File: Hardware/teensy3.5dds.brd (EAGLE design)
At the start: 110 x 85 mm, 102 parts, among them IC1 AD8034, IC10 AD8034, IC11 AD8034, IC12 AD8034, IC2 AD8034, IC4 AD737KRZ-R7, IC8 AD8034, IC9 AD8034, J1 1776275-2, J2 1776275-2, Q1 CSM-7X-DU, X1 1-227161-0

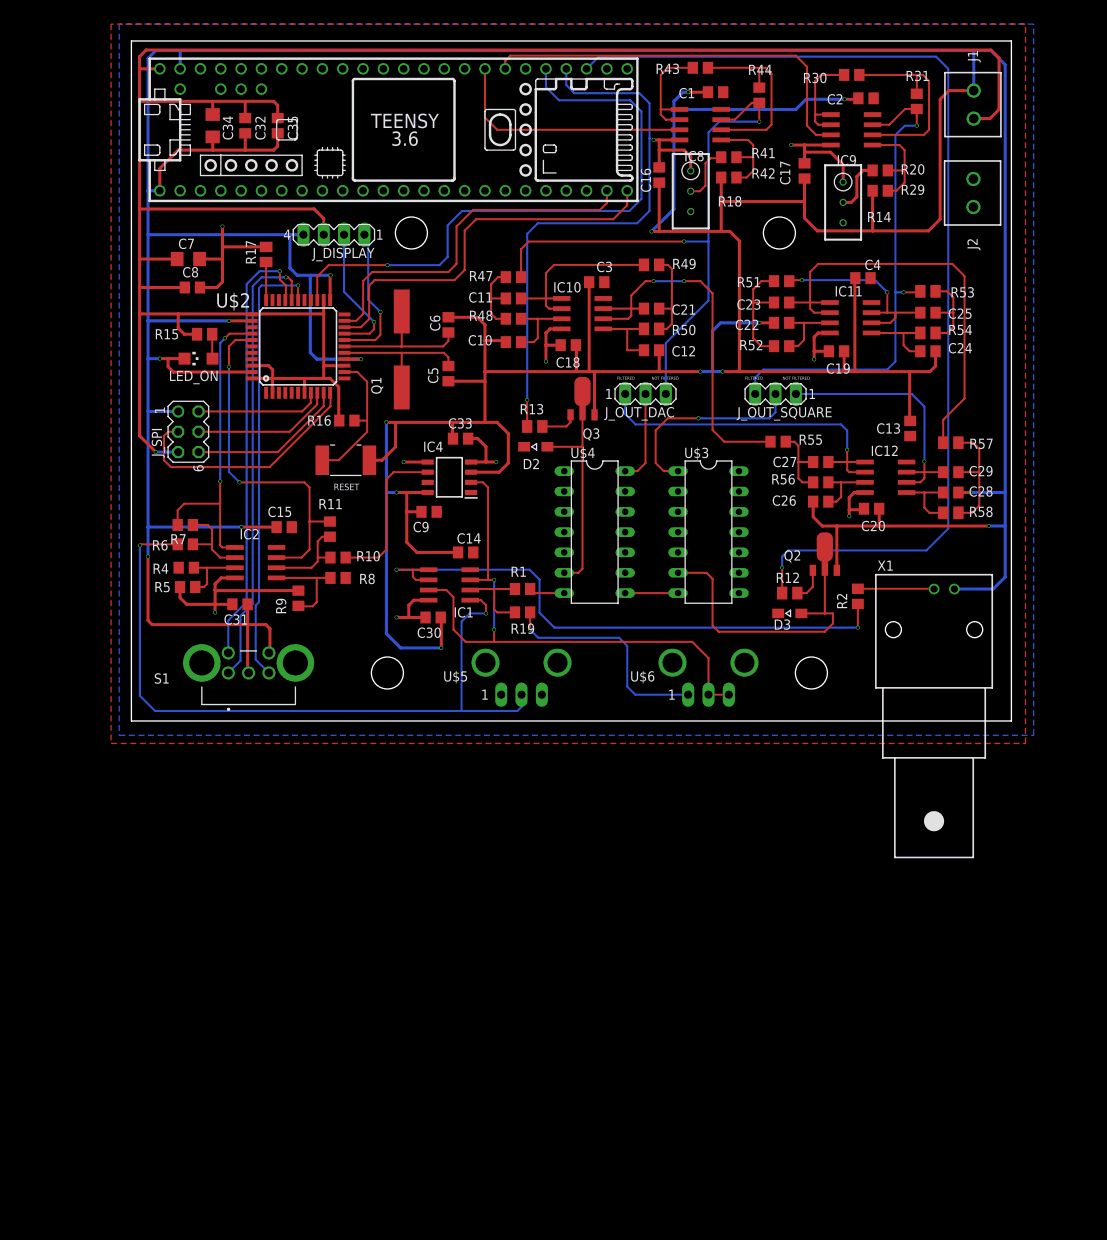
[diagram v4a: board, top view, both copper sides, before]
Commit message: hardware: renumber parts * Label power connector on board
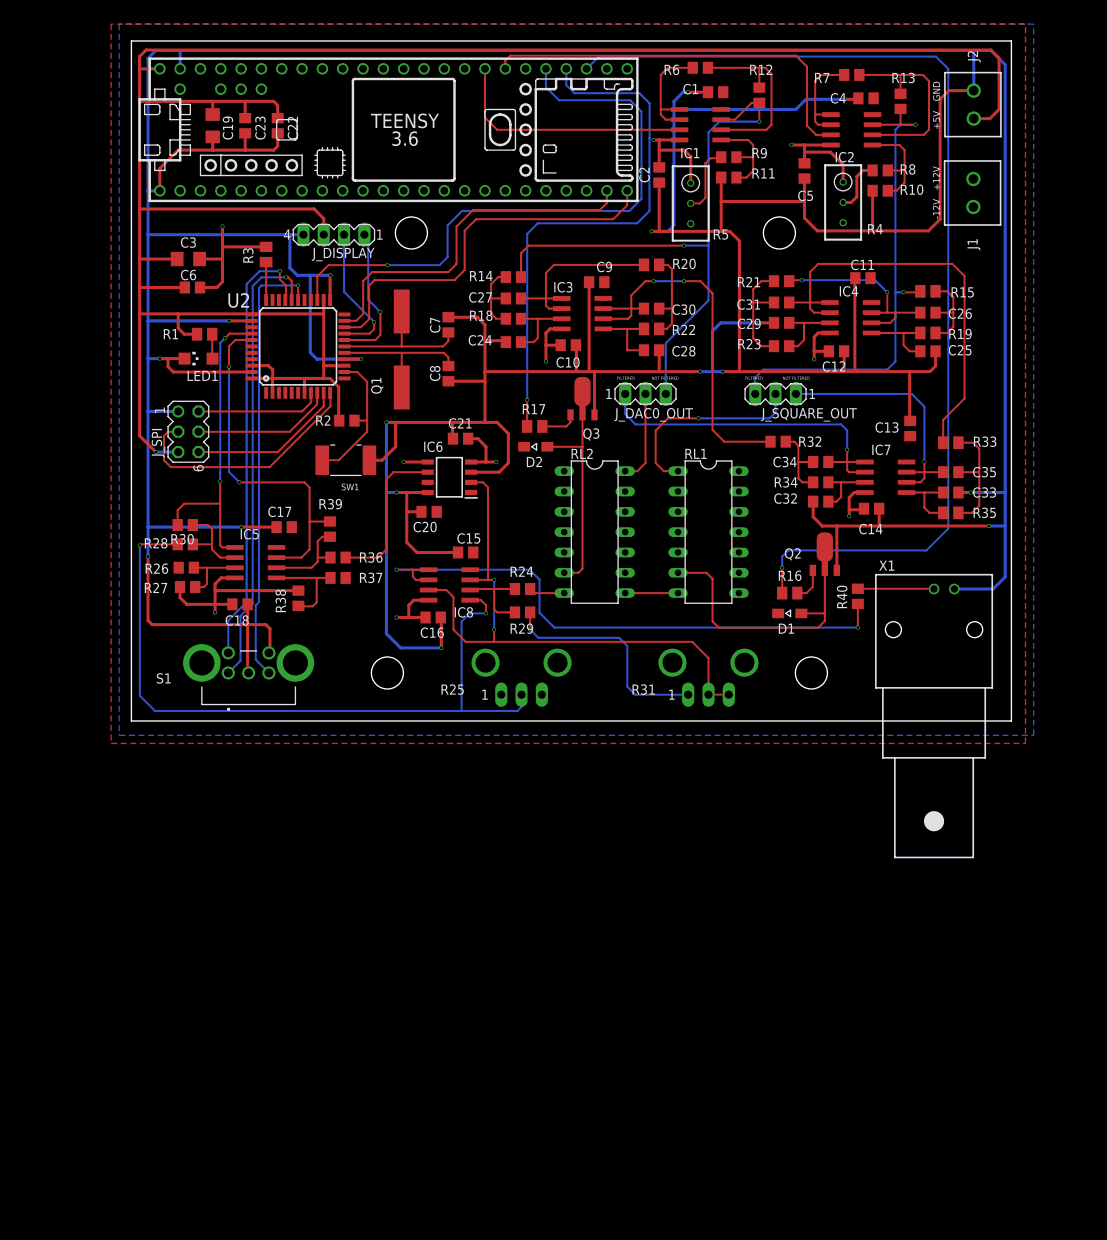
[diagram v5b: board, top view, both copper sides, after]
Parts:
- removed IC11, IC9: AD8034, linear:SO08
- removed R41, R42, R43, R44, R47, R48: (no value), rcl:R0805
- removed R49, R53, R54: (no value), rcl:M0805
- removed U$6: POTENTIOMETER_VERTICAL, Potentiometer_vertical:MA03-1
- added IC5: AD8034, linear:SO08
- added IC6: AD737KRZ-R7, AD737KRZ-R7:SOIC127P600X175-8N
- added R24, R26, R27, R28, R36, R37, R38, R39, R40: (no value), rcl:R0805
- added R3: 10kOhm, rcl:M0805
- C19: value (none) -> 100n; device rcl:C0805 -> rcl:C1206
- C22, C23: value (none) -> 100n
- C3: value (none) -> 1u; device rcl:C0805 -> rcl:C1206
- C32, C35: value 100n -> (none)
- C34: value 100n -> (none); device rcl:C1206 -> rcl:C0805
- C5: value 22pF -> (none)
- C6: value 22pF -> 1u
- C7: value 1u -> 22pF; device rcl:C1206 -> rcl:C0805
- C8: value 1u -> 22pF
- IC4: value AD737KRZ-R7 -> AD8034; device AD737KRZ-R7:SOIC127P600X175-8N -> linear:SO08
- R1: value (none) -> 220Ohm; device rcl:R0805 -> rcl:M0805
- R12, R13: device rcl:M0805 -> rcl:R0805
- R14, R18: device rcl:RTRIM3296W -> rcl:R0805
- R15: value 220Ohm -> (none)
- R16: value 10kOhm -> (none); device rcl:R0805 -> rcl:M0805
- R17: value 10kOhm -> (none)
- R19, R20: device rcl:R0805 -> rcl:M0805
- R2: value (none) -> 10kOhm
- R31: value (none) -> POTENTIOMETER_VERTICAL; device rcl:R0805 -> Potentiometer_vertical:MA03-1
- R4, R5: device rcl:R0805 -> rcl:RTRIM3296W
- moved R30 100.5 mm to (6.73, 39.5), turned to 0 degrees
- moved R7 100.5 mm to (90.0, 95.8), turned to 180 degrees
- moved C35 94.6 mm to (102.4, 46.1), turned to 180 degrees
- moved R4 93.9 mm to (89.0, 79.8)
- moved IC2 92.1 mm to (90.0, 88.9)
- moved R15 90.6 mm to (99.6, 68.7), turned to 0 degrees
- moved R6 87.7 mm to (71.1, 96.6), turned to 180 degrees
- moved C34 86.9 mm to (86.2, 47.4), turned to 180 degrees
- moved C32 85.9 mm to (86.2, 42.4), turned to 0 degrees
- moved R8 84.8 mm to (93.6, 83.8), turned to 0 degrees
- moved C19 82.9 mm to (10.2, 89.4), turned to 270 degrees
- moved R10 81.8 mm to (93.6, 81.3), turned to 0 degrees
- moved R5 79.1 mm to (69.9, 79.7), turned to 180 degrees
- moved C17 78.8 mm to (19.1, 39.2), turned to 180 degrees
- moved R31 78.6 mm to (72.1, 18.3), turned to 0 degrees
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- renumbered D3 to D1, IC10 to IC3, IC12 to IC7, J_OUT_DAC to J_DAC0_OUT, J_OUT_SQUARE to J_SQUARE_OUT, LED_ON to LED1, R50 to R22, R51 to R21, R52 to R23, R55 to R32, R56 to R34, R57 to R33, R58 to R35, RESET to SW1, U$1 to U1, U$2 to U2, U$3 to RL1, U$4 to RL2, U$5 to R25
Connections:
- net +5V: now also C19.1, C22.1, C23.1, C3.1, C6.1, J2.1, R1.2, R2.2; no longer C32.1, C34.1, C35.1, C7.1, C8.1, J1.1, R15.2, R16.2
- net AMPL_MEASURE: now also IC5.7, R39.2; no longer IC2.7, R11.2
- net DAC0: now also IC1.3; no longer IC8.3
- net DAC0_FILTERED: now also C34.1; no longer C27.1
- net DAC0_OFFSET: now also IC1.7, R12.1, R14.1; no longer IC8.7, R44.1, R47.1
- net DAC0_SEL: now also R17.1; no longer R13.1
- net GND: now also C11.2, C14.1, C17.2, C19.2, C2.1, C20.2, C21.1, C22.2, C23.2, C25.1, C29.1, C32.1, C6.2, C7.1, C8.1, IC6.3, IC6.8, J2.2, R10.1, R11.1, R3.2; no longer C14.2, C17.1, C19.1, C2.2, C20.1, C22.1, C26.1, C30.1, C31.1, C32.2, C34.2, C35.2, C6.1, C7.2, C8.2, IC4.3, IC4.8, J1.2, R17.2, R29.1, R42.1
- net N$10: now also R24.1; no longer R1.1
- net N$11: now also IC5.2, R28.2, R30.2; no longer IC2.2, R6.2, R7.2
- net N$13: now also IC5.3, R26.1, R27.2; no longer IC2.3, R4.1, R5.2
- net N$14: now also IC6.6, R36.1; no longer IC4.6, R10.1
- net N$15: now also R29.2, R31.1; no longer R19.2, U$6.1
- net N$16: now also IC5.6, R36.2, R39.1; no longer IC2.6, R10.2, R11.1
- net N$17: now also R16.2; no longer R12.2
- net N$18: now also R17.2; no longer R13.2
- net N$19: now also IC8.1, IC8.2, R40.1; no longer IC1.1, IC1.2, R2.1
- net N$22: now also IC5.5, R37.2, R38.1; no longer IC2.5, R8.2, R9.1
- net N$3: now also IC8.5, R28.1; no longer IC1.5, R6.1
- net N$30: now also R1.1; no longer R15.1
- net N$31: now also C7.2; no longer C6.2
- net N$32: now also R3.1; no longer R17.1
- net N$35: now also R2.1; no longer R16.1
- net N$38: now also IC2.1, IC2.2, R7.2; no longer IC9.1, IC9.2, R30.2
- net N$4: now also C8.2; no longer C5.2
- net N$41: now also IC1.1, IC1.2, R6.2; no longer IC8.1, IC8.2, R43.2
- net N$5: now also IC8.6, R24.2, R29.1; no longer IC1.6, R1.2, R19.1
- net N$50: now also C27.2, R14.2, R18.1; no longer C11.2, R47.2, R48.1
- net N$51: now also IC1.6, R12.2, R6.1; no longer IC8.6, R43.1, R44.2
- net N$53: now also C27.1, R20.1; no longer C11.1, R49.1
- net N$54: now also IC1.5, R11.2, R9.2; no longer IC8.5, R41.2, R42.2
- net N$56: now also R5.2, R9.1; no longer R18.2, R41.1
- net N$57: now also IC2.6, R13.2, R7.1; no longer IC9.6, R30.1, R31.2
- net N$58: now also C24.2, R18.2; no longer C10.2, R48.2
- net N$59: now also IC2.5, R10.2, R8.2; no longer IC9.5, R20.2, R29.2
- net N$6: now also R40.2; no longer R2.2
- net N$60: now also R4.2, R8.1; no longer R14.2, R20.1
- net N$61: now also C30.1, R20.2; no longer C21.1, R49.2
- net N$62: now also C30.2; no longer C21.2
- net N$63: now also C28.2; no longer C12.2
- net N$66: now also C31.2; no longer C23.2
- net N$67: now also C31.1, IC4.1, IC4.2; no longer C23.1, IC11.1, IC11.2
- net N$68: now also C29.2, IC4.3; no longer C22.2, IC11.3
- net N$69: now also C26.1, R15.2, R19.1; no longer C25.1, R53.2, R54.1
- net N$70: now also C26.2, IC4.6, IC4.7; no longer C25.2, IC11.6, IC11.7
- net N$71: now also C25.2, IC4.5, R19.2; no longer C24.2, IC11.5, R54.2
- net N$73: now also C34.2; no longer C27.2
- net N$75: now also C32.2; no longer C26.2
- net N$76: now also C35.1; no longer C29.1
- net N$78: now also C33.2; no longer C28.2
- net N$9: now also IC6.2, IC8.3, IC8.7, R31.2, R31.3; no longer IC1.3, IC1.7, IC4.2, U$6.2, U$6.3
- net OFF_MEASURE: now also IC5.1, R30.1; no longer IC2.1, R7.1
- net SQUARE: now also IC2.3; no longer IC9.3
- net SQUARE_FILTERED: now also C35.2; no longer C29.2
- net SQUARE_OFFSET: now also IC2.7, R13.1, R15.1; no longer IC9.7, R31.1, R53.1
- net SQUARE_SEL: now also R16.1; no longer R12.1
- net V+: now also C11.1, C17.1, C20.1, IC4.8, IC5.8, IC6.7, J1.2, R26.2, R37.1, R4.3, R5.3; no longer C14.1, C2.1, C3.1, IC11.8, IC4.7, IC9.8, J2.2, R14.3, R18.3, R4.2, R8.1
- net V-: now also C10.2, C12.2, C14.2, C2.2, C21.2, C5.2, IC5.4, IC6.4, IC6.5, J1.1, R27.1, R38.2, R4.1; no longer C17.2, C19.2, C20.2, C30.2, C31.2, C33.2, IC11.4, IC4.5, IC9.4, J2.1, R14.1, R18.1, R9.2
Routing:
- net N$2: track 37.1 -> 34.2 mm
- net V-: track 92.1 -> 93.6 mm
- net N$56: track 7.21 -> 8.74 mm
- net GND: track 844.5 -> 845.6 mm
- net SQUARE_OFFSET: track 63.5 -> 62.7 mm
- net DAC0_OFFSET: track 77.1 -> 76.6 mm
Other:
- board text added: "+12V"
- board text added: "+5V"
- board text added: "-12V"
- board text added: "GND"

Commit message: little fixes
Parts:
- added R41, R42, R43: (no value), rcl:R0805
- C1, C10, C12, C13, C14, C15, C16, C17, C18, C2, C20, C21, C4, C5, C9: value (none) -> 100n
- C23: value 100n -> 1u
- C24, C25, C28, C29, C32, C33: value (none) -> 10p
- C26, C27, C30, C31, C34, C35: value (none) -> 100p
- C6: value 1u -> 100n
- C7, C8: value 22pF -> 22p
- Q1: value CSM-7X-DU -> 10MHz
- R1: value 220Ohm -> 220
- R10, R11, R12, R24, R6, R7, R8, R9: value (none) -> 1k
- R13: value (none) -> 100k; device rcl:R0805 -> rcl:RTRIM3296W
- R14, R18: value (none) -> 2.74k
- R15: value (none) -> 130
- R19: value (none) -> 4.75k
- R2, R3: value 10kOhm -> 10k
- R20: value (none) -> 787
- R21: value (none) -> 150
- R22: value (none) -> 14.3k
- R23: value (none) -> 3.74k
- R25, R31: value POTENTIOMETER_VERTICAL -> 10k
- R29: value (none) -> 100
- R32: value (none) -> 562
- R33: value (none) -> 243
- R34: value (none) -> 20k
- R35: value (none) -> 1.78k
- R4: value (none) -> 1k; device rcl:RTRIM3296W -> rcl:R0805
- R40: value (none) -> 50
- R5: value (none) -> 100k
- moved R7 147.8 mm to (3.56, -24.1), turned to 0 degrees
- moved R8 137.9 mm to (7.75, -24.1)
- moved IC2 137.9 mm to (1.91, -17.1), turned to 0 degrees
- moved R4 137.2 mm to (-0.64, -24.1), turned to 0 degrees
- moved R13 137.0 mm to (1.91, -6.99), turned to 0 degrees
- moved R10 128.7 mm to (8.38, -15.1)
- moved S1 44.0 mm to (-7.49, -17.9), turned to 0 degrees
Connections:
- removed net N$1: S1.3, U2.28
- removed net N$38: IC2.1, IC2.2, R7.2
- removed net N$41: IC1.1, IC1.2, R6.2
- removed net N$57: IC2.6, R13.2, R7.1
- removed net N$59: IC2.5, R10.2, R8.2
- removed net N$60: R4.2, R8.1
- new net N$20: R13.2, R4.1
- new net N$23: IC1.1, IC1.2, R11.1
- new net N$24: IC2.6, R10.2, R8.1
- new net N$27: IC2.1, IC2.2, R7.1
- new net N$28: IC2.5, R4.2, R7.2
- new net N$29: R43.2, S1.5, U2.29
- new net V-1: R13.1
- net +5V: now also R41.1, R42.1
- net GND: now also R43.1, R6.2, R8.2, S1.6, S1.7; no longer R10.1, R11.1
- net N$25: now also R41.2, S1.1; no longer S1.5
- net N$8: now also R42.2, S1.3, U2.12; no longer S1.1, U2.29
- net SQUARE_OFFSET: now also R10.1; no longer R13.1
- net V+: now also R13.3; no longer R4.3
- net V-: no longer R4.1
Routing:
- net N$8: track 57.5 -> 0.00 mm, vias 1 -> 0
- net N$25: track 55.8 -> 0.00 mm, vias 1 -> 0
- net N$1: track 55.8 -> 0.00 mm, vias 1 -> 0
- net N$57: track 24.8 -> 0.00 mm
- net N$21: track 23.6 -> 0.00 mm
- net N$41: track 14.3 -> 0.00 mm
- net GND: track 845.6 -> 831.8 mm
- net N$38: track 13.1 -> 0.00 mm
- net N$59: track 12.9 -> 0.00 mm
- net N$26: track 12.0 -> 0.00 mm
- net N$23: track 0.00 -> 7.45 mm
- net N$60: track 6.83 -> 0.00 mm
- net SQUARE_OFFSET: track 62.7 -> 57.1 mm
- net DAC0_OFFSET: track 76.6 -> 73.3 mm
- net N$70: track 25.5 -> 22.9 mm
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
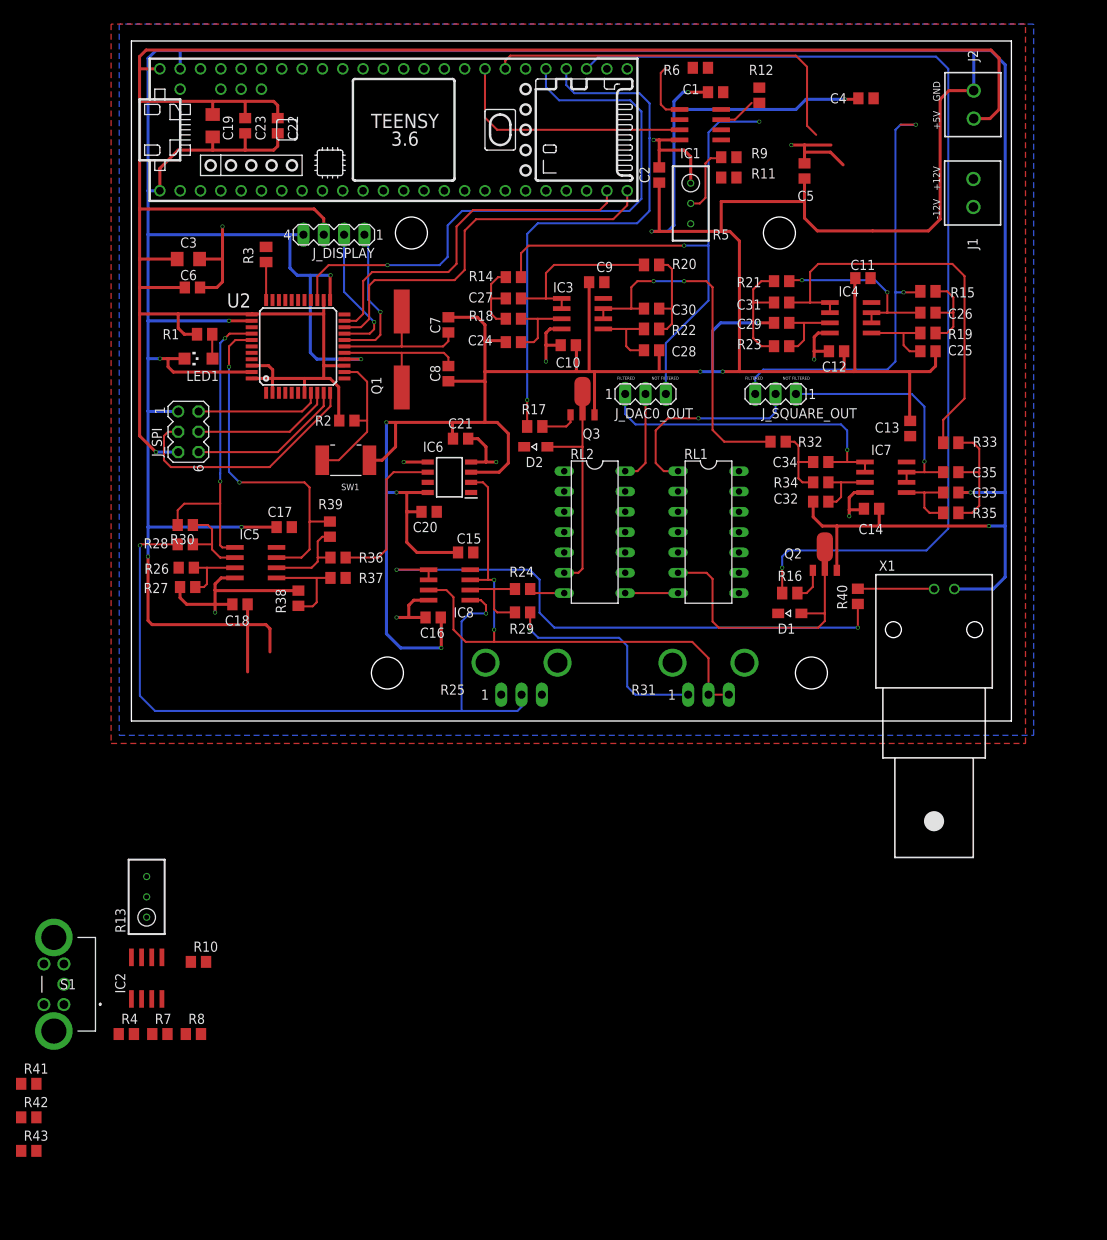
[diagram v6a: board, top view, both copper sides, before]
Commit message: an actually working filter for the square wave
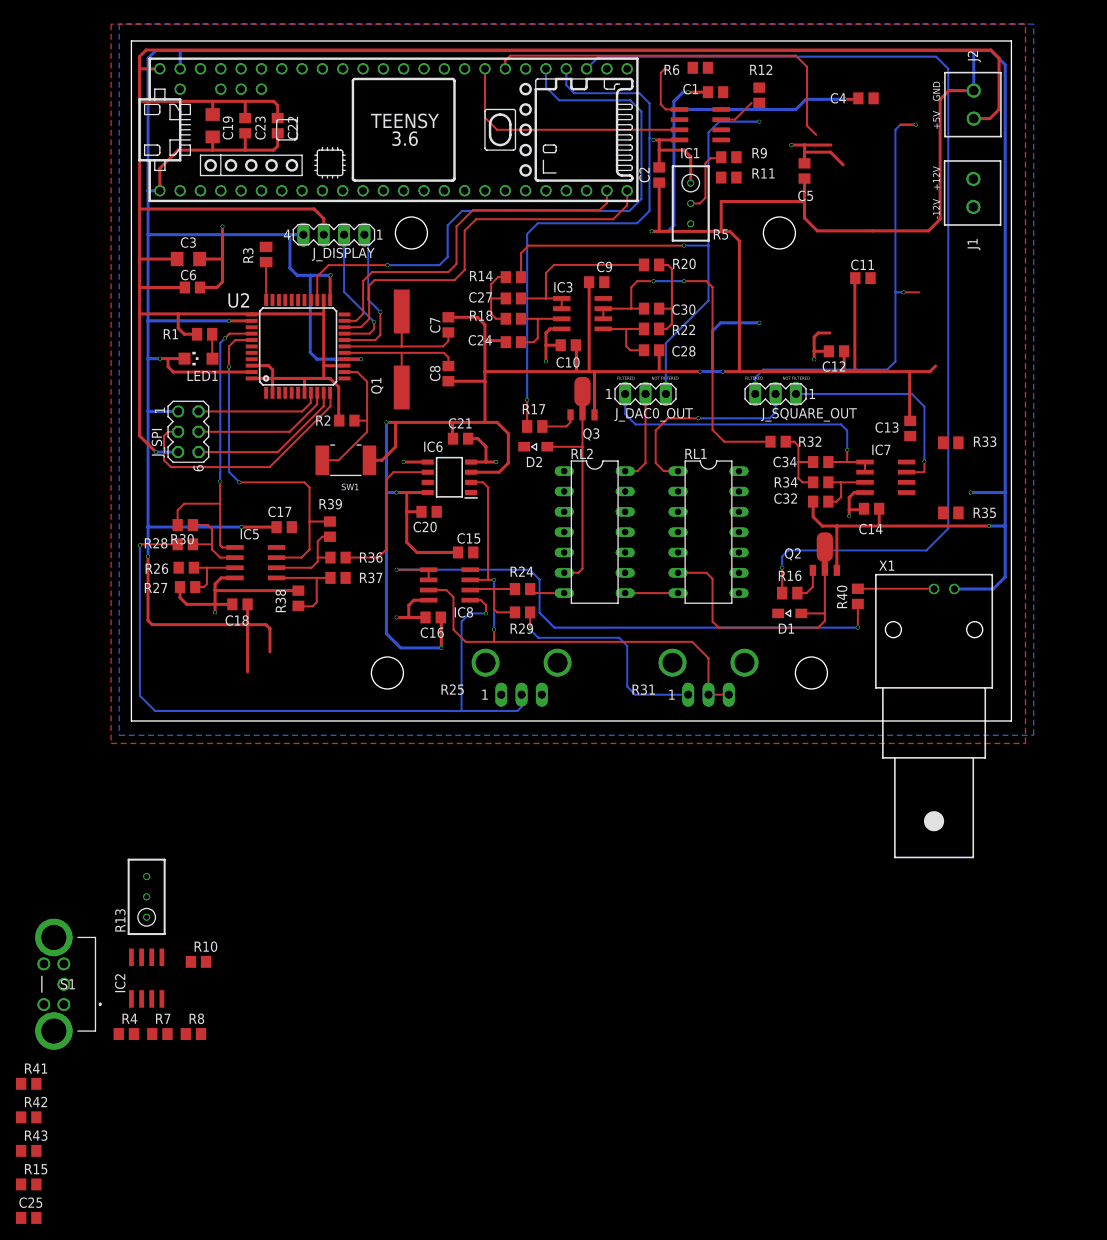
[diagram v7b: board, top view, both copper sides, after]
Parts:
- removed C26, C31, C35: 100p, rcl:C0805
- removed C29, C33: 10p, rcl:C0805
- removed IC4: AD8034, linear:SO08
- removed R19: 4.75k, rcl:M0805
- removed R21: 150, rcl:R0805
- removed R23: 3.74k, rcl:R0805
- C25: value 10p -> (none)
- R15: value 130 -> (none); device rcl:M0805 -> rcl:R0805
- moved R15 158.4 mm to (-12.8, -42.9)
- moved C25 156.1 mm to (-12.8, -47.1), turned to 0 degrees
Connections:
- removed net N$66: C31.2, R21.2, R23.1
- removed net N$67: C31.1, IC4.1, IC4.2, R33.1
- removed net N$68: C29.2, IC4.3, R23.2
- removed net N$69: C26.1, R15.2, R19.1
- removed net N$70: C26.2, IC4.6, IC4.7, R21.1
- removed net N$71: C25.2, IC4.5, R19.2
- removed net N$76: C35.1, R33.2, R35.1
- removed net N$78: C33.2, IC7.5, R35.2
- new net N$1: IC7.5, R33.2, R35.1
- new net N$34: C25.2, R15.1, R33.1
- net GND: now also IC7.6; no longer C29.1, C33.1
- net SQUARE_FILTERED: now also R35.2; no longer C35.2, IC7.6
- net SQUARE_OFFSET: now also R15.2; no longer R15.1
- net V+: no longer IC4.8
- net V-: no longer IC4.4
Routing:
- net N$67: track 52.5 -> 0.00 mm
- net N$70: track 22.9 -> 0.00 mm, vias 2 -> 0
- net N$76: track 15.6 -> 0.00 mm
- net N$66: track 14.8 -> 0.00 mm
- net N$69: track 11.0 -> 0.00 mm
- net N$71: track 10.0 -> 0.00 mm
- net N$68: track 9.40 -> 0.00 mm
- net N$78: track 9.10 -> 0.00 mm
- net GND: track 831.8 -> 826.6 mm
- net SQUARE_FILTERED: track 30.8 -> 27.1 mm
